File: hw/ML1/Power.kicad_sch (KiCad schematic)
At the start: 5 parts, among them U3 NCP1117-3.3_SOT223

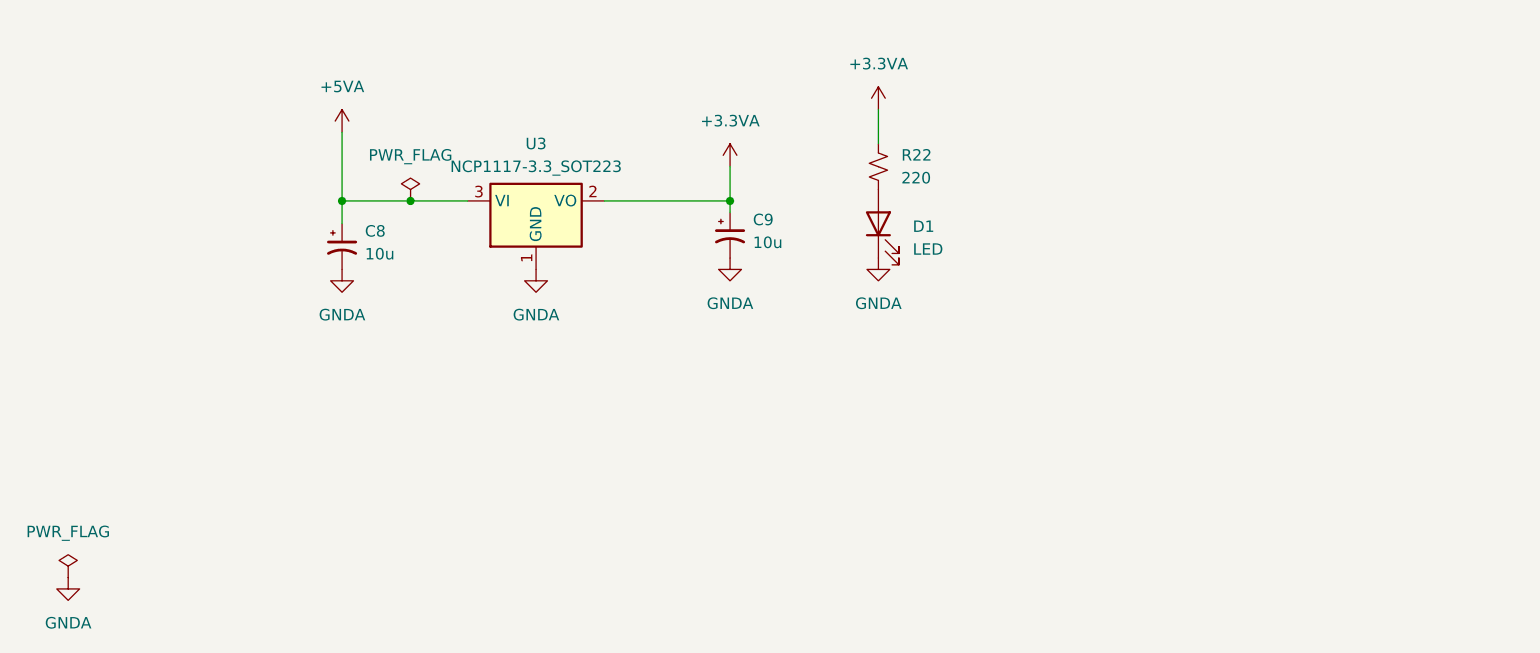
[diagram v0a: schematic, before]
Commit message: Re-work of ML1 board in process
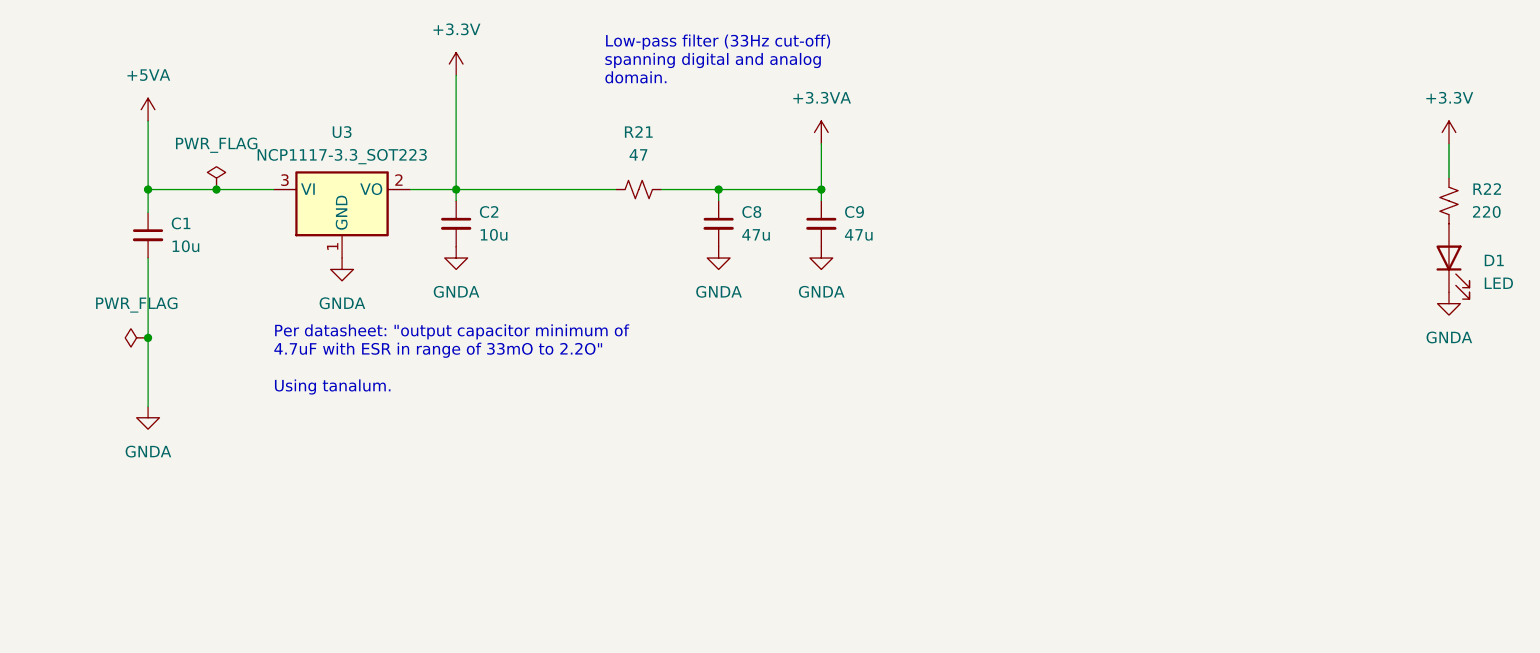
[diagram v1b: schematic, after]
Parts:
- removed C8, C9: 10u, KiCad-Library:CAP_KEMET_530_530, symbol Device:C_Polarized_Small_US
- added C1, C2: 10u, Capacitor_SMD:C_0805_2012Metric_Pad1.18x1.45mm_HandSolder, symbol Device:C_Small
- added C8, C9: 47u, Capacitor_SMD:C_0805_2012Metric_Pad1.18x1.45mm_HandSolder, symbol Device:C_Small
- added R21: 47, Resistor_SMD:R_0805_2012Metric_Pad1.20x1.40mm_HandSolder, symbol Device:R_Small_US
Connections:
- net +3.3VA: now also C8.1, C9.1, R21.2; no longer R22.1, U3.2 (VO)
- net +5VA: now also C1.1
- net GNDA: now also C1.2, C2.2, C8.2, C9.2
- new net +3.3V: C2.1, R21.1, R22.1, U3.2 (VO)
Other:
- note added: "Low-pass filter (33Hz cut-off) spanning digital and analog domain."
- note added: "Per datasheet: "output capacitor minimum of 4.7uF with ESR in range of 33mO to 2.2O" Using tanalum."
- moved on the sheet: D1, R22, U3

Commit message: First draft of board is passing DRC
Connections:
- net +3.3V: no longer R22.1
- net +3.3VA: now also R22.1

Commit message: Final checks, preparing to create GRB
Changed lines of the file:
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@@
 			)
 		)
-		(property "Description" ""
+		(property "Description" "Power symbol creates a global label with name \"GNDA\" , analog ground"
 			(at 80.01 87.63 0)
 			(effects
@@
 			)
 		)
-		(property "Description" ""
+		(property "Description" "Special symbol for telling ERC where power comes from"
 			(at 58.42 96.52 0)
 			(effects
@@
 			)
 		)
-		(property "Description" ""
+		(property "Description" "Power symbol creates a global label with name \"GNDA\" , analog ground"
 			(at 58.42 104.14 0)
 			(effects
@@
 			)
 		)
-		(property "Description" ""
+		(property "Description" "Power symbol creates a global label with name \"+3.3VA\""
 			(at 133.35 74.93 0)
 			(effects
@@
 			)
 		)
-		(property "Description" ""
+		(property "Description" "Power symbol creates a global label with name \"GNDA\" , analog ground"
 			(at 121.92 86.36 0)
 			(effects
@@
 			)
 		)
-		(property "Description" ""
+		(property "Description" "Power symbol creates a global label with name \"GNDA\" , analog ground"
 			(at 92.71 86.36 0)
 			(effects
@@
 			)
 		)
-		(property "Description" ""
+		(property "Description" "Unpolarized capacitor, small symbol"
 			(at 92.71 83.82 0)
 			(effects
@@
 			)
 		)
-		(property "Description" ""
+		(property "Description" "Power symbol creates a global label with name \"+5VA\""
 			(at 58.42 72.39 0)
 			(effects
@@
 			)
 		)
-		(property "Description" ""
+		(property "Description" "Unpolarized capacitor, small symbol"
 			(at 121.92 83.82 0)
 			(effects
@@
 			)
 		)
-		(property "Description" ""
+		(property "Description" "Unpolarized capacitor, small symbol"
 			(at 133.35 83.82 0)
 			(effects
@@
 			)
 		)
-		(property "Description" ""
+		(property "Description" "1A Low drop-out regulator, Fixed Output 3.3V, SOT-223"
 			(at 80.01 80.01 0)
 			(effects
@@
 			)
 		)
-		(property "Description" ""
+		(property "Description" "Unpolarized capacitor, small symbol"
 			(at 58.42 85.09 0)
 			(effects
@@
 			)
 		)
-		(property "Description" ""
+		(property "Description" "Resistor, small US symbol"
 			(at 203.2 81.28 0)
 			(effects
@@
 			)
 		)
-		(property "Description" ""
+		(property "Description" "Light emitting diode"
 			(at 203.2 87.63 0)
 			(effects
@@
 			)
 		)
-		(property "Description" ""
+		(property "Description" "Power symbol creates a global label with name \"GNDA\" , analog ground"
 			(at 133.35 86.36 0)
 			(effects
@@
 			)
 		)
-		(property "Description" ""
+		(property "Description" "Resistor, small US symbol"
 			(at 113.03 80.01 0)
 			(effects
@@
 				(path "/5f8f636b-fd0e-498e-8696-0a023acb4c09/b1678fb4-46a9-4663-81fd-d1aa3cb2b4fa"
 					(reference "R21")
+					(unit 1)
+				)
+			)
+		)
+	)
+	(symbol
+		(lib_id "power:PWR_FLAG")
+		(at 133.35 80.01 270)
+		(unit 1)
+		(exclude_from_sim no)
+		(in_bom yes)
+		(on_board yes)
+		(dnp no)
+		(fields_autoplaced yes)
+		(property "Reference" "#FLG04"
+			(at 135.255 80.01 0)
+			(effects
+				(font
+					(size 1.27 1.27)
+				)
+				(hide yes)
+			)
+		)
+		(property "Value" "PWR_FLAG"
+			(at 137.16 80.0099 90)
+			(effects
+				(font
+					(size 1.27 1.27)
+				)
+				(justify left)
+			)
+		)
+		(property "Footprint" ""
+			(at 133.35 80.01 0)
+			(effects
+				(font
+					(size 1.27 1.27)
+				)
+				(hide yes)
+			)
+		)
+		(property "Datasheet" "~"
+			(at 133.35 80.01 0)
+			(effects
+				(font
+					(size 1.27 1.27)
+				)
+				(hide yes)
+			)
+		)
+		(property "Description" "Special symbol for telling ERC where power comes from"
+			(at 133.35 80.01 0)
+			(effects
+				(font
+					(size 1.27 1.27)
+				)
+				(hide yes)
+			)
+		)
+		(pin "1"
+		)
+		(instances
+			(project "ML1"
+				(path "/5f8f636b-fd0e-498e-8696-0a023acb4c09/b1678fb4-46a9-4663-81fd-d1aa3cb2b4fa"
+					(reference "#FLG04")
 					(unit 1)
 				)
@@
 			)
 		)
-		(property "Description" ""
+		(property "Description" "Special symbol for telling ERC where power comes from"
 			(at 66.04 80.01 0)
 			(effects
@@
 	)
 	(symbol
-		(lib_name "+3.3VA_1")
 		(lib_id "power:+3.3VA")
 		(at 203.2 74.93 0)
@@
 			)
 		)
-		(property "Description" ""
+		(property "Description" "Power symbol creates a global label with name \"GNDA\" , analog ground"
 			(at 203.2 91.44 0)
 			(effects
@@
 			)
 		)
-		(property "Description" ""
+		(property "Description" "Power symbol creates a global label with name \"+3.3V\""
 			(at 92.71 67.31 0)
 			(effects
